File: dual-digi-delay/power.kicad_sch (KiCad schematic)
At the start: 7 parts, among them U9 LM7805_TO220

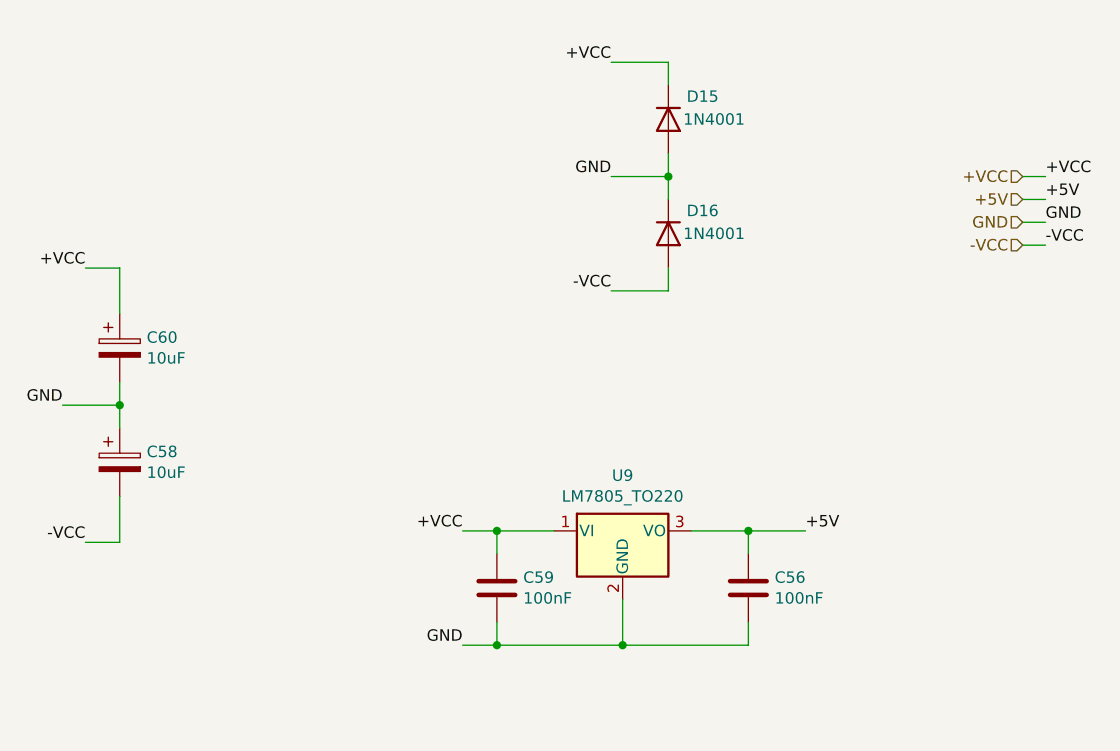
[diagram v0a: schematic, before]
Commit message: Making temporary branch for rev2 builds
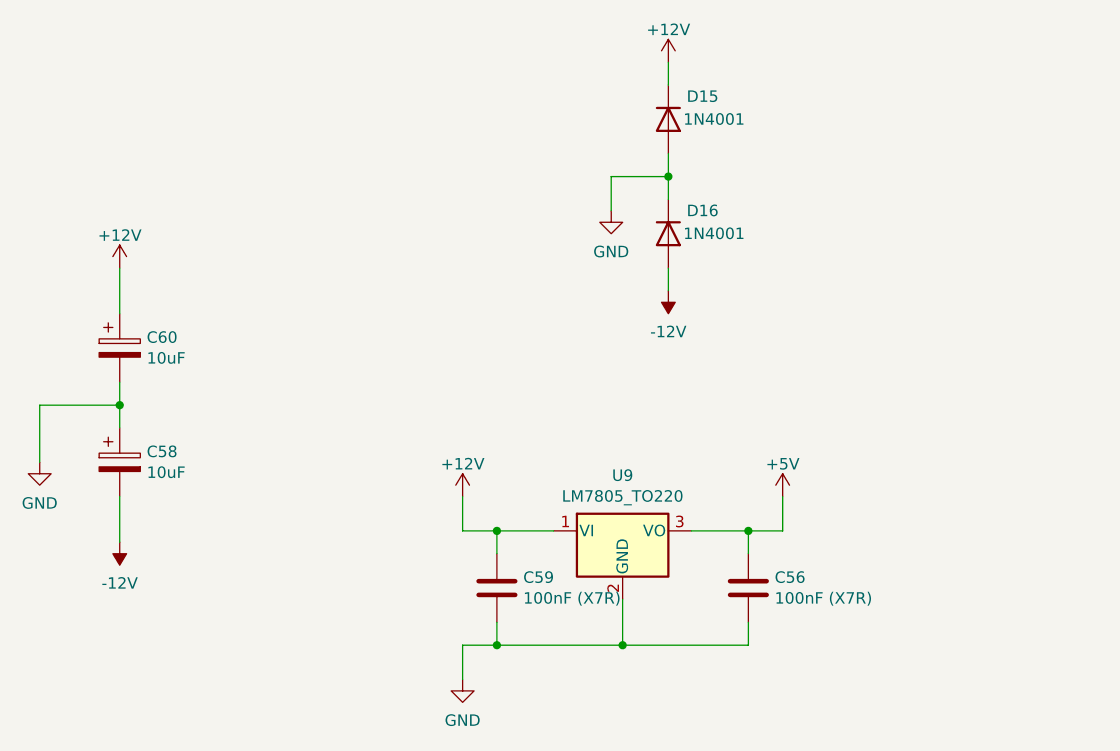
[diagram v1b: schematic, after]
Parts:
- C56, C59: value 100nF -> 100nF (X7R)
- D15, D16: now left out of the parts list
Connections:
- net +VCC renamed +12V
- net -VCC renamed -12V
